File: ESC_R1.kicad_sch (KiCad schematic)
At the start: 0 parts

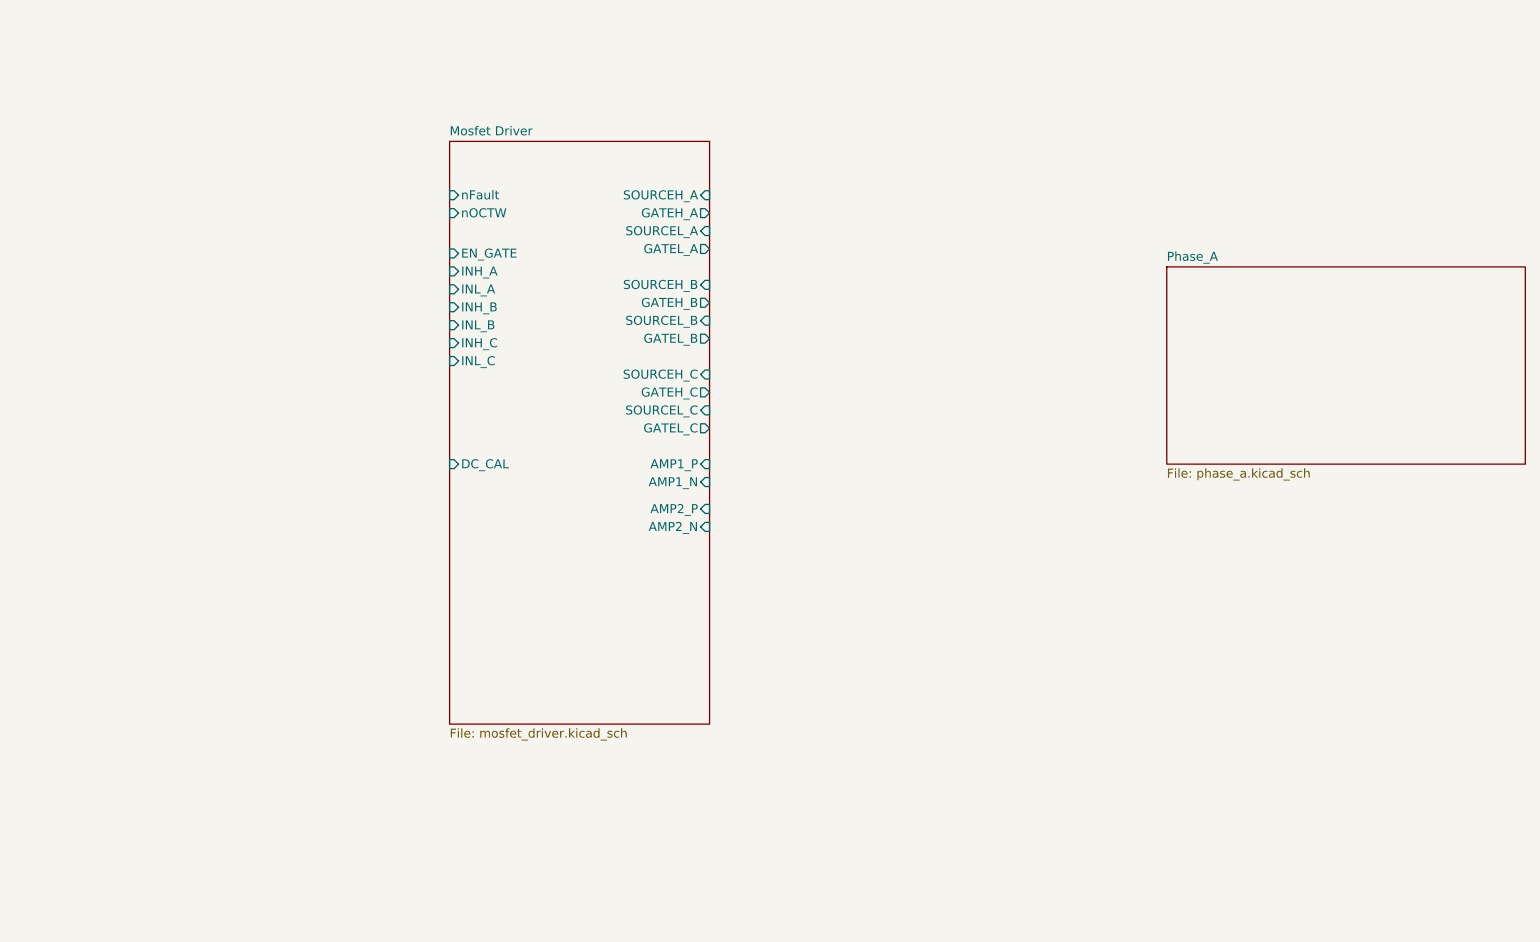
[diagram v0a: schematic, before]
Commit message: feat: added power source schematics and updated capacitor values
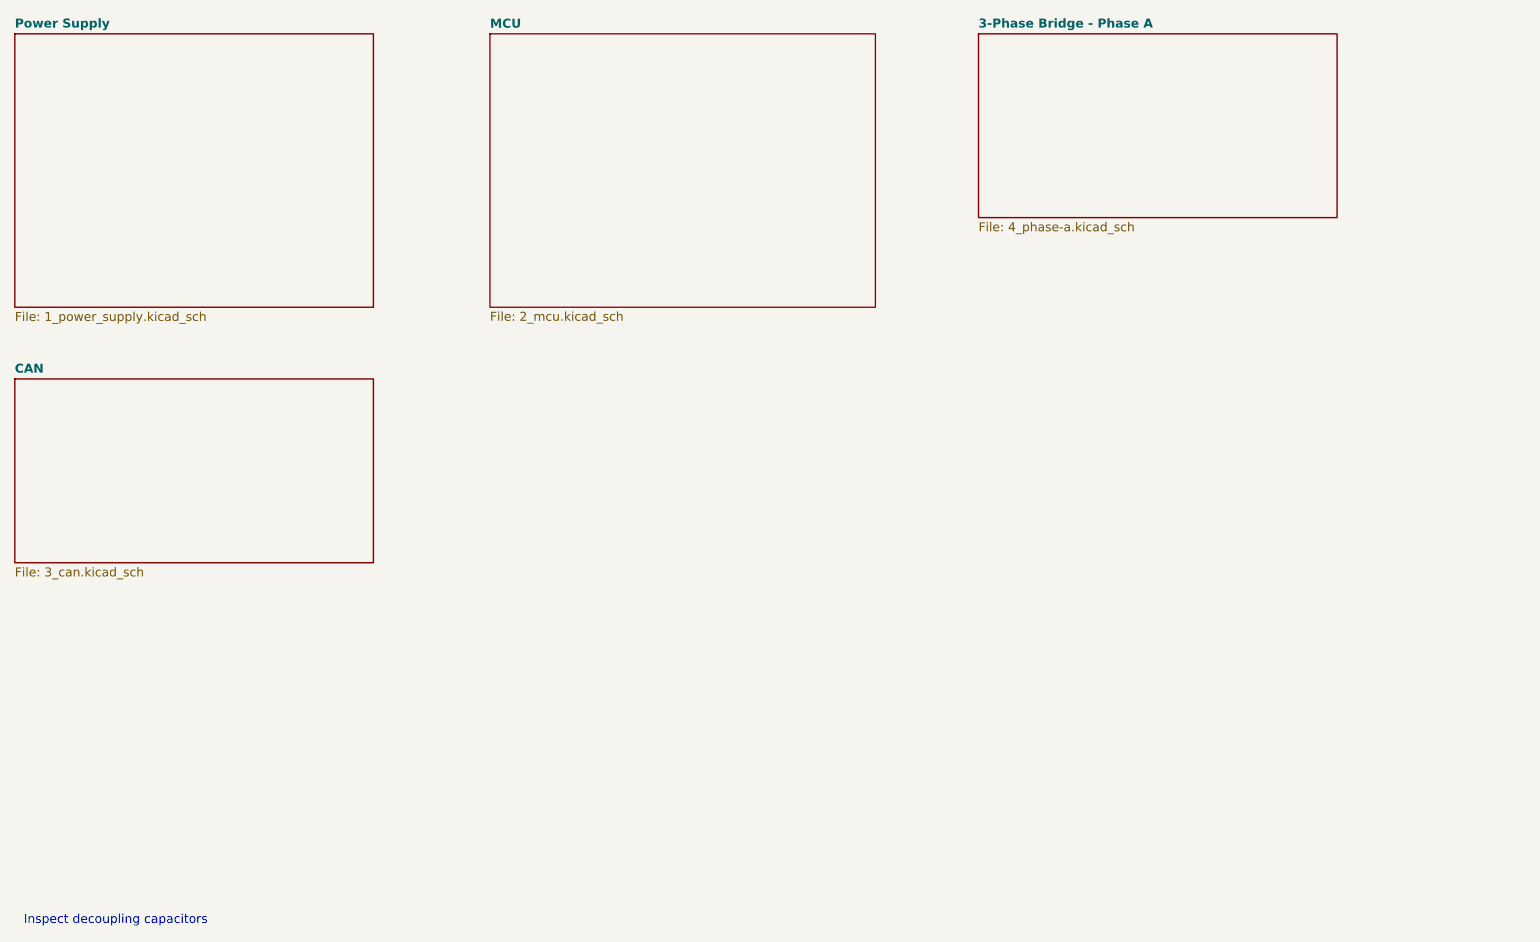
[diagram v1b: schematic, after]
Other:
- sheet Phase_A renamed 3-Phase Bridge - Phase A
- removed sheet Mosfet Driver
- added sheet CAN (3_can.kicad_sch)
- added sheet MCU (2_mcu.kicad_sch)
- added sheet Power Supply (1_power_supply.kicad_sch)
- sheet 3-Phase Bridge - Phase A: file phase_a.kicad_sch -> 4_phase-a.kicad_sch
- note added: "Inspect decoupling capacitors"

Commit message: feat: power supply updates and mcu kickoff
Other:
- note removed: "Inspect decoupling capacitors"
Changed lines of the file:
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@@
     (rev "1.0")
   )
-  (text "Inspect decoupling capacitors" (at 43.815 163.195 0)
-    (effects (font (size 1.27 1.27)) (justify left bottom))
-  )
-  (sheet (at 109.855 36.83) (size 54.61 38.735) (fields_autoplaced)
+  (sheet (at 107.95 36.83) (size 54.61 38.735) (fields_autoplaced)
     (stroke (width 0.1524) (type solid) (color 0 0 0 0))
     (fill (color 0 0 0 0.0000))
-    (property "Sheet name" "MCU" (id 0) (at 109.855 36.1184 0)
+    (property "Sheet name" "MCU" (id 0) (at 107.95 36.1184 0)
       (effects (font (size 1.27 1.27) bold) (justify left bottom))
     )
-    (property "Sheet file" "2_mcu.kicad_sch" (id 1) (at 109.855 76.1496 0)
+    (property "Sheet file" "2_mcu.kicad_sch" (id 1) (at 107.95 76.1496 0)
       (effects (font (size 1.27 1.27)) (justify left top))
     )
   )
-  (sheet (at 179.07 36.83) (size 50.8 26.035) (fields_autoplaced)
+  (sheet (at 175.895 36.83) (size 50.8 26.035) (fields_autoplaced)
     (stroke (width 0.2) (type solid) (color 0 0 0 0))
     (fill (color 0 0 0 0.0000))
-    (property "Sheet name" "3-Phase Bridge - Phase A" (id 0) (at 179.07 36.0946 0)
+    (property "Sheet name" "3-Phase Bridge - Phase A" (id 0) (at 175.895 36.0946 0)
       (effects (font (size 1.27 1.27) bold) (justify left bottom))
     )
-    (property "Sheet file" "4_phase-a.kicad_sch" (id 1) (at 179.07 63.4734 0)
+    (property "Sheet file" "4_phase-a.kicad_sch" (id 1) (at 175.895 63.4734 0)
       (effects (font (size 1.27 1.27)) (justify left top))
     )
@@
       (reference "#PWR?") (unit 1) (value "+BATT") (footprint "")
     )
+    (path "/52041989-aba3-4113-ba04-ece39669328f/ec6f6915-698e-4568-8091-a2a0f18c2f67"
+      (reference "#PWR?") (unit 1) (value "GND") (footprint "")
+    )
     (path "/bab0431c-ca33-4c57-9dbe-00ccaf05ca0f/ef6ddf44-7721-4d49-8cfe-704dcfb60b7c"
       (reference "#PWR?") (unit 1) (value "GND") (footprint "")
@@
       (reference "C?") (unit 1) (value "10u") (footprint "")
     )
+    (path "/bab0431c-ca33-4c57-9dbe-00ccaf05ca0f/0b170aa7-5d18-4a73-9916-a0b34d6dcbc7"
+      (reference "C?") (unit 1) (value "100u") (footprint "")
+    )
     (path "/bab0431c-ca33-4c57-9dbe-00ccaf05ca0f/3129d89f-c610-49f2-a3bb-75dd041f3eb5"
       (reference "C?") (unit 1) (value "8n2") (footprint "")
@@
       (reference "U?") (unit 1) (value "TLV75533PDBV") (footprint "Package_TO_SOT_SMD:SOT-23-5")
     )
-  )
+    (path "/52041989-aba3-4113-ba04-ece39669328f/baed0279-7574-4779-9614-21514ca50e72"
+      (reference "U?") (unit 1) (value "STM32F446RETx") (footprint "Package_QFP:LQFP-64_10x10mm_P0.5mm")
+    )
+  )

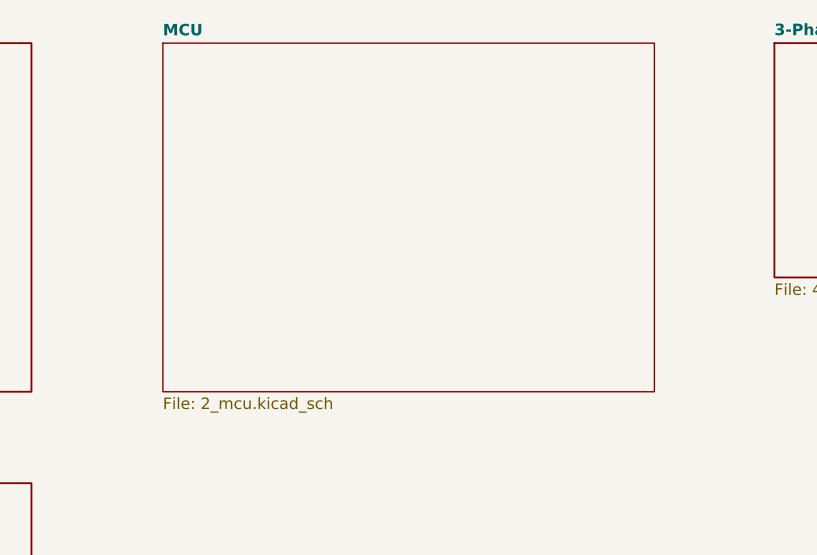
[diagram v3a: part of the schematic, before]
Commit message: feat: initial peripheral circuitry for MCU
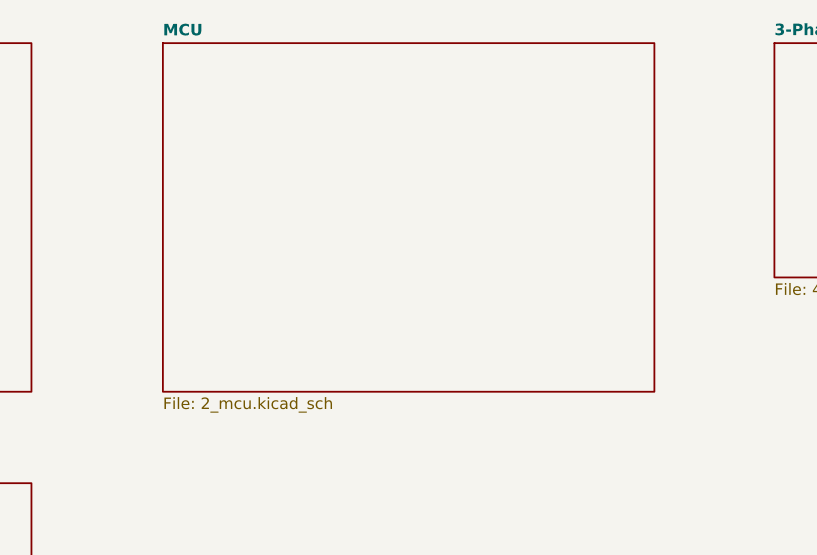
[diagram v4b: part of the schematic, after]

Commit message: feat: USB circuitry
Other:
- added sheet USB (4_usb.kicad_sch)
- sheet 3-Phase Bridge - Phase A: file 4_phase-a.kicad_sch -> 5_phase-a.kicad_sch
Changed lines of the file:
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@@
     (rev "1.0")
+  )
+  (sheet (at 42.545 121.285) (size 50.8 26.035) (fields_autoplaced)
+    (stroke (width 0.2) (type solid))
+    (fill (color 0 0 0 0.0000))
+    (property "Sheetname" "USB" (at 42.545 120.5496 0)
+      (effects (font (size 1.27 1.27) bold) (justify left bottom))
+    )
+    (property "Sheetfile" "4_usb.kicad_sch" (at 42.545 147.9284 0)
+      (effects (font (size 1.27 1.27)) (justify left top))
+    )
+    (instances
+      (project "ESC_R1"
+        (path "/9dea2e18-5867-4ed4-a12d-7ee109225de0" (page "5"))
+      )
+    )
   )
   (sheet (at 107.95 36.83) (size 54.61 38.735) (fields_autoplaced)
@@
       (effects (font (size 1.27 1.27) bold) (justify left bottom))
     )
-    (property "Sheetfile" "4_phase-a.kicad_sch" (at 175.895 63.4734 0)
+    (property "Sheetfile" "5_phase-a.kicad_sch" (at 175.895 63.4734 0)
       (effects (font (size 1.27 1.27)) (justify left top))
     )

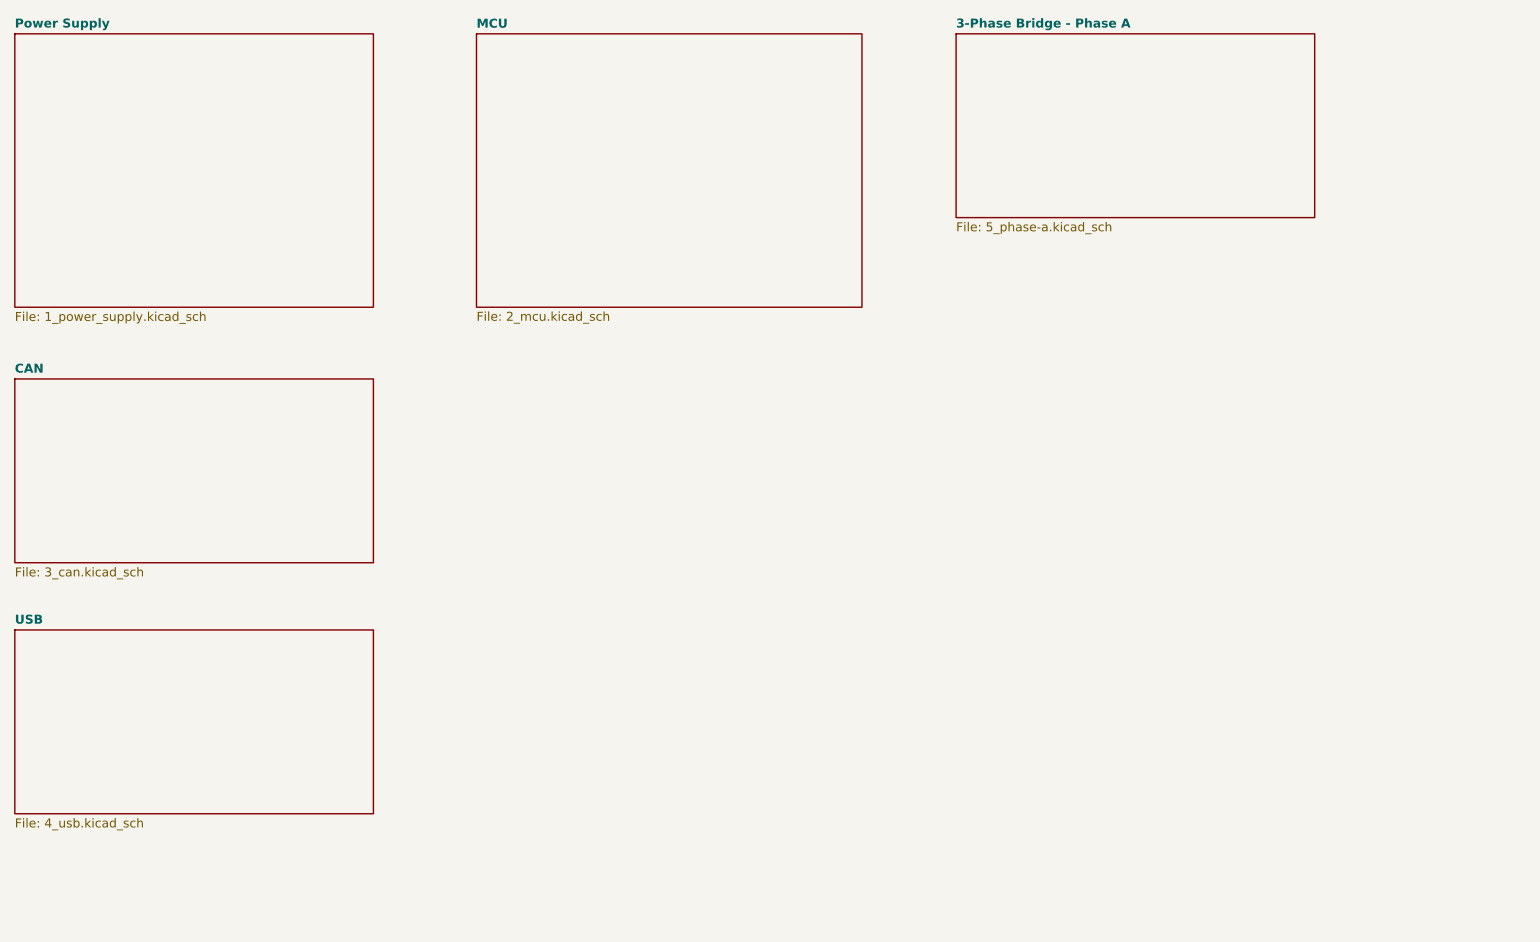
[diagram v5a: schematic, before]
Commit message: chore: updated links and footprints
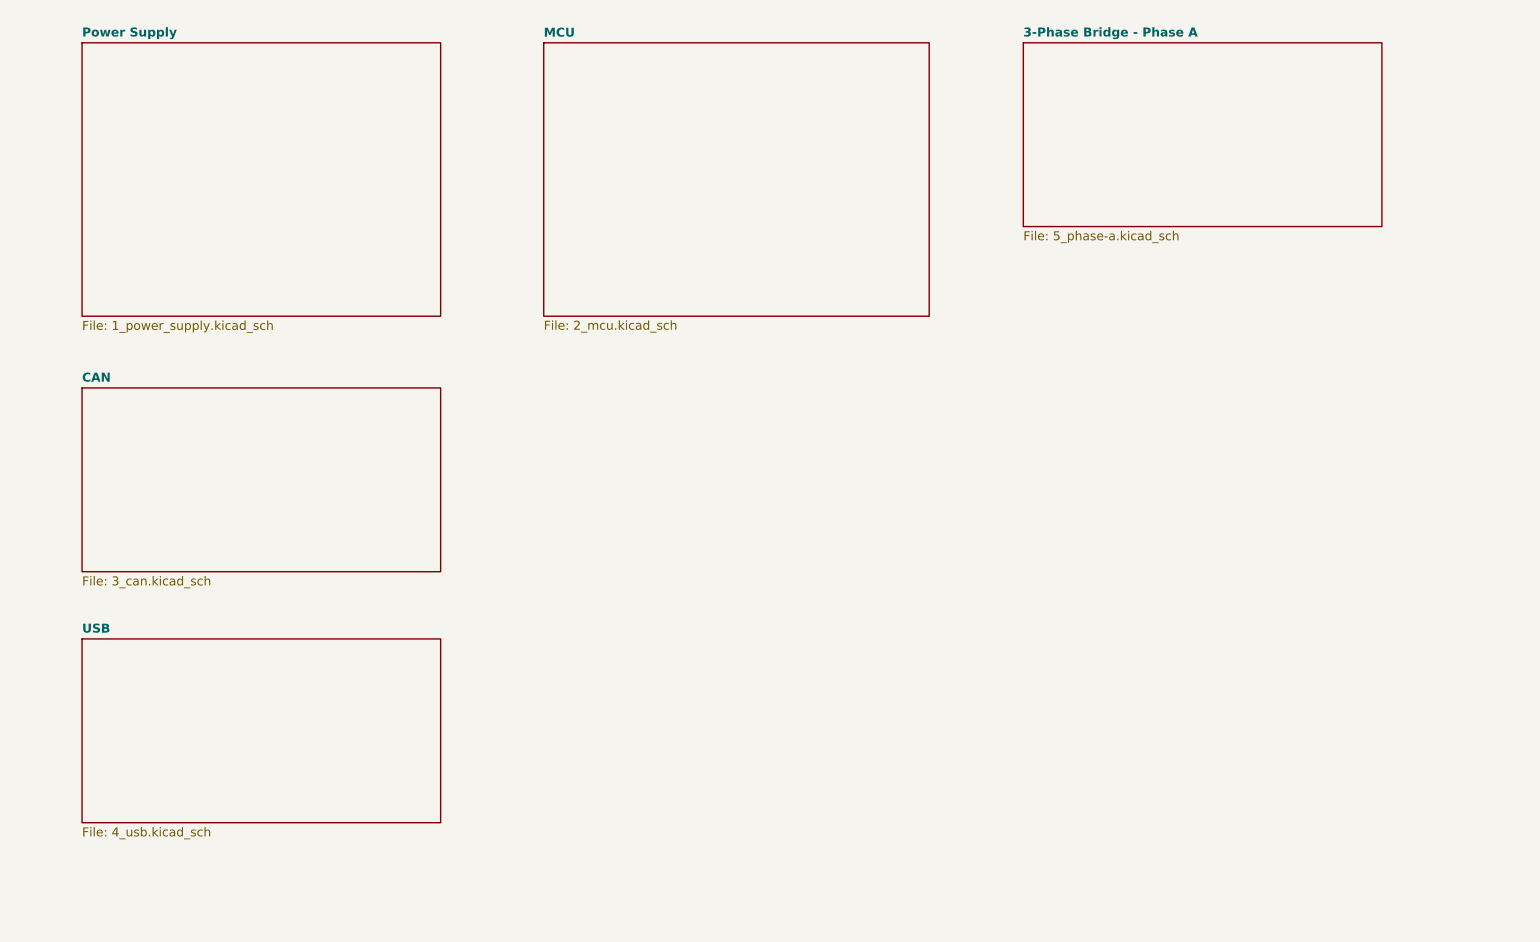
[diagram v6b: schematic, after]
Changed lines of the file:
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@@
     (rev "1.0")
   )
-  (sheet (at 42.545 121.285) (size 50.8 26.035) (fields_autoplaced)
+  (sheet (at 52.07 122.555) (size 50.8 26.035) (fields_autoplaced)
     (stroke (width 0.2) (type solid))
     (fill (color 0 0 0 0.0000))
-    (property "Sheetname" "USB" (at 42.545 120.5496 0)
+    (property "Sheetname" "USB" (at 52.07 121.8196 0)
       (effects (font (size 1.27 1.27) bold) (justify left bottom))
     )
-    (property "Sheetfile" "4_usb.kicad_sch" (at 42.545 147.9284 0)
+    (property "Sheetfile" "4_usb.kicad_sch" (at 52.07 149.1984 0)
       (effects (font (size 1.27 1.27)) (justify left top))
     )
@@
     )
   )
-  (sheet (at 107.95 36.83) (size 54.61 38.735) (fields_autoplaced)
+  (sheet (at 117.475 38.1) (size 54.61 38.735) (fields_autoplaced)
     (stroke (width 0.2) (type solid))
     (fill (color 0 0 0 0.0000))
-    (property "Sheetname" "MCU" (at 107.95 36.1184 0)
+    (property "Sheetname" "MCU" (at 117.475 37.3884 0)
       (effects (font (size 1.27 1.27) bold) (justify left bottom))
     )
-    (property "Sheetfile" "2_mcu.kicad_sch" (at 107.95 76.1496 0)
+    (property "Sheetfile" "2_mcu.kicad_sch" (at 117.475 77.4196 0)
       (effects (font (size 1.27 1.27)) (justify left top))
     )
@@
     )
   )
-  (sheet (at 175.895 36.83) (size 50.8 26.035) (fields_autoplaced)
+  (sheet (at 185.42 38.1) (size 50.8 26.035) (fields_autoplaced)
     (stroke (width 0.2) (type solid))
     (fill (color 0 0 0 0.0000))
-    (property "Sheetname" "3-Phase Bridge - Phase A" (at 175.895 36.0946 0)
+    (property "Sheetname" "3-Phase Bridge - Phase A" (at 185.42 37.3646 0)
       (effects (font (size 1.27 1.27) bold) (justify left bottom))
     )
-    (property "Sheetfile" "5_phase-a.kicad_sch" (at 175.895 63.4734 0)
+    (property "Sheetfile" "5_phase-a.kicad_sch" (at 185.42 64.7434 0)
       (effects (font (size 1.27 1.27)) (justify left top))
     )
@@
     )
   )
-  (sheet (at 42.545 85.725) (size 50.8 26.035) (fields_autoplaced)
+  (sheet (at 52.07 86.995) (size 50.8 26.035) (fields_autoplaced)
     (stroke (width 0.2) (type solid))
     (fill (color 0 0 0 0.0000))
-    (property "Sheetname" "CAN" (at 42.545 84.9896 0)
+    (property "Sheetname" "CAN" (at 52.07 86.2596 0)
       (effects (font (size 1.27 1.27) bold) (justify left bottom))
     )
-    (property "Sheetfile" "3_can.kicad_sch" (at 42.545 112.3684 0)
+    (property "Sheetfile" "3_can.kicad_sch" (at 52.07 113.6384 0)
       (effects (font (size 1.27 1.27)) (justify left top))
     )
@@
     )
   )
-  (sheet (at 42.545 36.83) (size 50.8 38.735) (fields_autoplaced)
+  (sheet (at 52.07 38.1) (size 50.8 38.735) (fields_autoplaced)
     (stroke (width 0.2) (type solid))
     (fill (color 0 0 0 0.0000))
-    (property "Sheetname" "Power Supply" (at 42.545 36.0946 0)
+    (property "Sheetname" "Power Supply" (at 52.07 37.3646 0)
       (effects (font (size 1.27 1.27) bold) (justify left bottom))
     )
-    (property "Sheetfile" "1_power_supply.kicad_sch" (at 42.545 76.1734 0)
+    (property "Sheetfile" "1_power_supply.kicad_sch" (at 52.07 77.4434 0)
       (effects (font (size 1.27 1.27)) (justify left top))
     )
